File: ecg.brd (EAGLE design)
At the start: 56 x 85 mm, 34 parts, among them IC1 ADP151, IC2 ADP151, U1 TMP102AIDRLT, U2 TMP102AIDRLT, U3 ADAS1000BSTZ

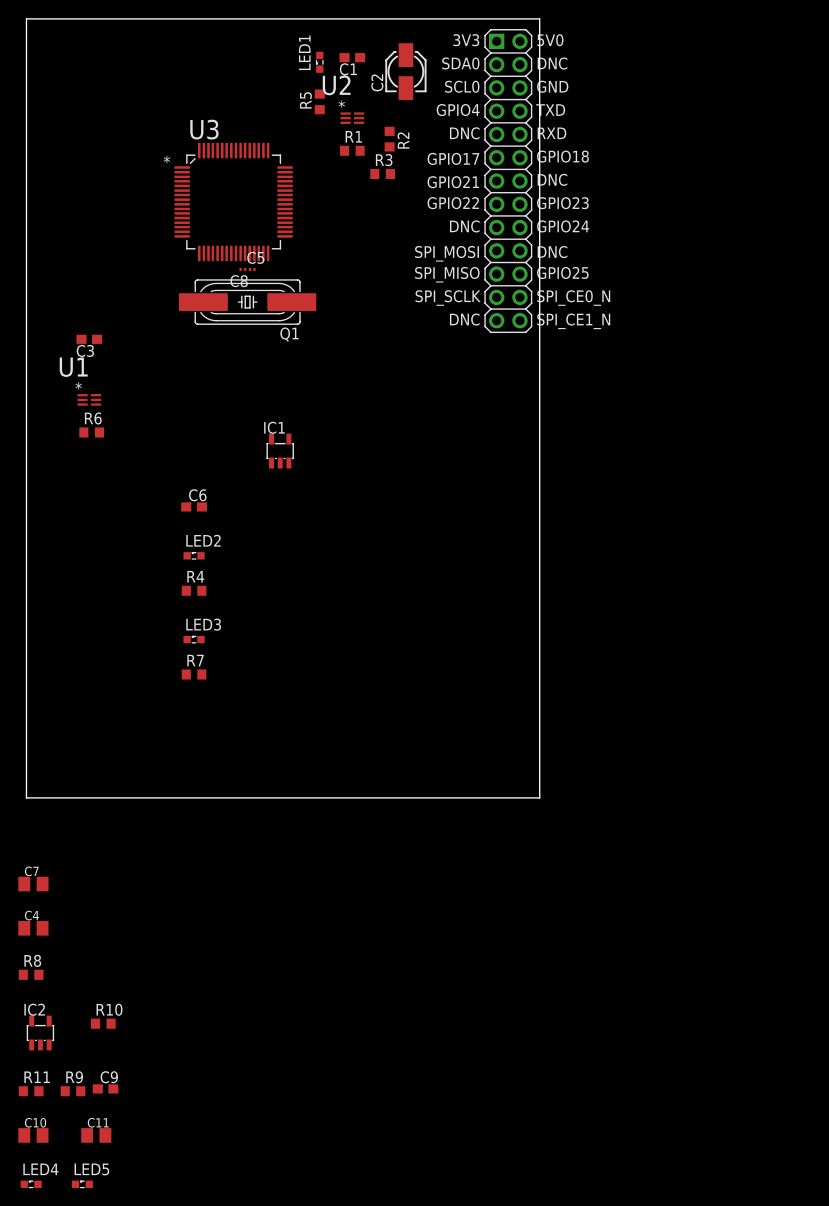
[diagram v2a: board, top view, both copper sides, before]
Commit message: The board is now horizontal
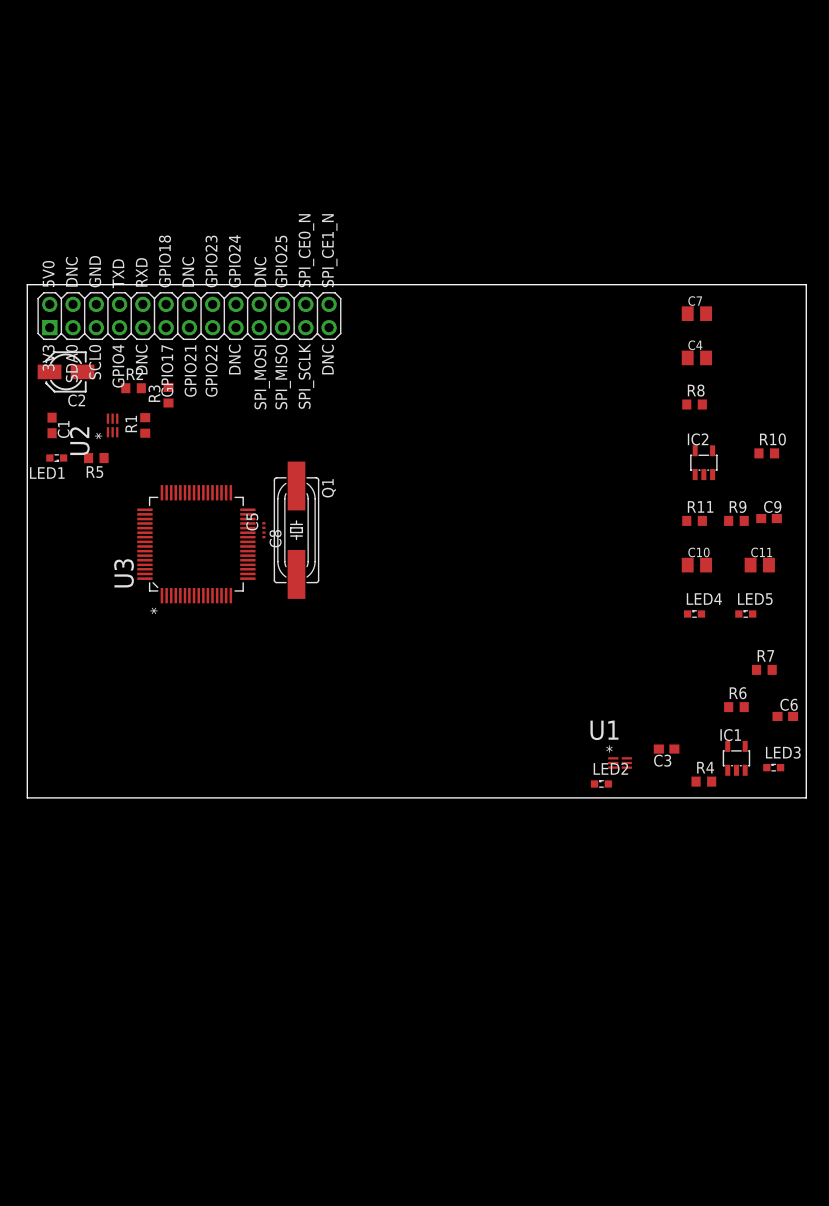
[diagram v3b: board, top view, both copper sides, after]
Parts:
- moved C10 95.5 mm to (73.2, 25.4)
- moved C11 95.5 mm to (80.0, 25.4)
- moved C4 95.5 mm to (73.2, 48.0)
- moved C7 95.5 mm to (73.2, 52.8)
- moved C9 95.5 mm to (81.0, 30.5)
- moved IC2 95.5 mm to (73.9, 36.6)
- moved LED4 95.5 mm to (72.9, 20.1)
- moved LED5 95.5 mm to (78.5, 20.1)
- moved R10 95.5 mm to (80.8, 37.6)
- moved R11 95.5 mm to (72.9, 30.2)
- moved R8 95.5 mm to (72.9, 42.9)
- moved R9 95.5 mm to (77.5, 30.2)
- moved RPI 85.1 mm to (85.1, 0.00), turned to 90 degrees
- moved C3 77.2 mm to (69.8, 5.33)
- moved R6 76.5 mm to (77.5, 9.91)
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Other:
- board size 56 x 85 mm -> 85 x 56 mm
